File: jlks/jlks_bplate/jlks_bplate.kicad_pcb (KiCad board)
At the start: 2 copper layers, 114.3 x 99.4 mm, 5 parts

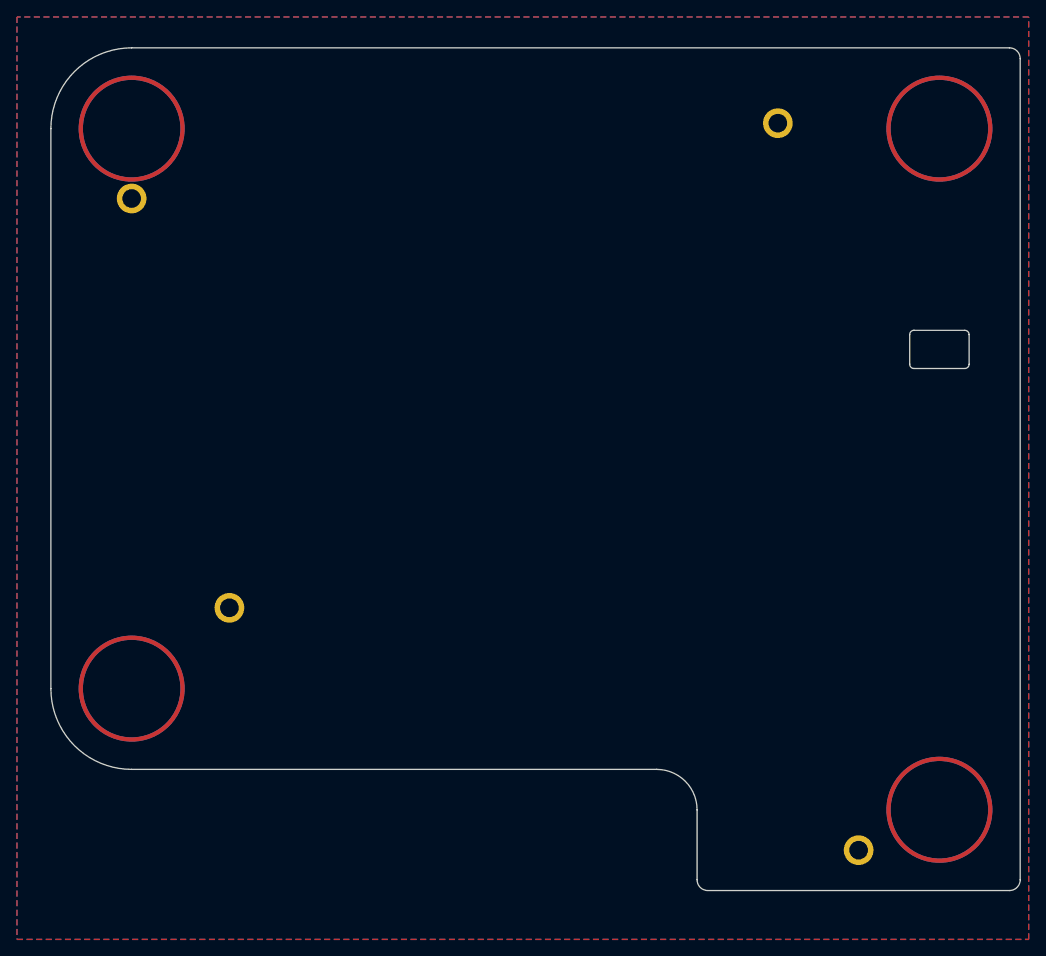
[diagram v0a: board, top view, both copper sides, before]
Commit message: Moved some of the mounting holes around.
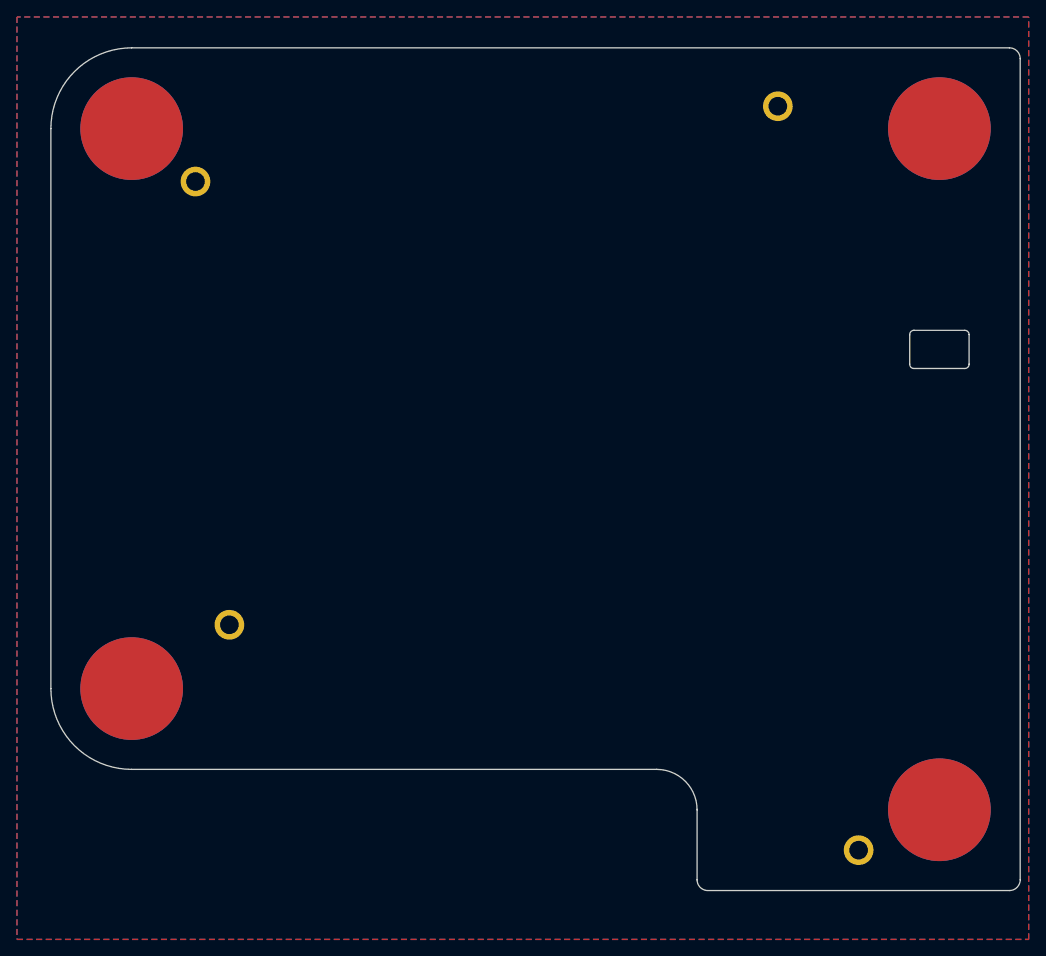
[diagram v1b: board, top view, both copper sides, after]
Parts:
- moved H1 7.79 mm to (74.2, 64.0)
- moved H0 2.00 mm to (142.9, 55.1)
- moved H2 2.00 mm to (78.2, 116.3)
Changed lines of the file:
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@@
   (net 1 "GND")
   (footprint "MountingHole:MountingHole_2.2mm_M2_ISO7380_Pad" (layer "F.Cu")
-    (at 78.2 114.3)
+    (at 78.2 116.3)
     (descr "Mounting Hole 2.2mm, M2, ISO7380")
     (tags "mounting hole 2.2mm m2 iso7380")
@@
   )
   (footprint "MountingHole:MountingHole_2.2mm_M2_ISO7380_Pad" (layer "F.Cu")
-    (at 142.875 57.15)
+    (at 142.875 55.15)
     (descr "Mounting Hole 2.2mm, M2, ISO7380")
     (tags "mounting hole 2.2mm m2 iso7380")
@@
   )
   (footprint "MountingHole:MountingHole_2.2mm_M2_ISO7380_Pad" (layer "F.Cu")
-    (at 66.675 66.033161)
+    (at 74.2 64.033161)
     (descr "Mounting Hole 2.2mm, M2, ISO7380")
     (tags "mounting hole 2.2mm m2 iso7380")
@@
   )
   (gr_circle (center 161.925 138.1125) (end 167.925 138.1125)
-    (stroke (width 0.5) (type default)) (fill none) (layer "F.Cu"))
+    (stroke (width 0.1) (type solid)) (fill solid) (layer "F.Cu"))
   (gr_circle (center 66.675 57.791839) (end 72.675 57.791839)
-    (stroke (width 0.5) (type default)) (fill none) (layer "F.Cu"))
+    (stroke (width 0.1) (type solid)) (fill solid) (layer "F.Cu"))
   (gr_circle (center 66.675 123.825) (end 72.675 123.825)
-    (stroke (width 0.5) (type default)) (fill none) (layer "F.Cu"))
+    (stroke (width 0.1) (type solid)) (fill solid) (layer "F.Cu"))
   (gr_circle (center 161.925 57.791839) (end 167.925 57.791839)
-    (stroke (width 0.5) (type default)) (fill none) (layer "F.Cu"))
+    (stroke (width 0.1) (type solid)) (fill solid) (layer "F.Cu"))
   (gr_circle (center 66.675 123.825) (end 72.675 123.825)
-    (stroke (width 0.5) (type default)) (fill none) (layer "B.Cu"))
+    (stroke (width 0.1) (type solid)) (fill solid) (layer "B.Cu"))
   (gr_circle (center 161.925 138.1125) (end 167.925 138.1125)
-    (stroke (width 0.5) (type default)) (fill none) (layer "B.Cu"))
+    (stroke (width 0.1) (type solid)) (fill solid) (layer "B.Cu"))
   (gr_circle (center 66.675 57.791839) (end 72.675 57.791839)
-    (stroke (width 0.5) (type default)) (fill none) (layer "B.Cu"))
+    (stroke (width 0.1) (type solid)) (fill solid) (layer "B.Cu"))
   (gr_circle (center 161.925 57.791839) (end 167.925 57.791839)
-    (stroke (width 0.5) (type default)) (fill none) (layer "B.Cu"))
+    (stroke (width 0.1) (type solid)) (fill solid) (layer "B.Cu"))
   (gr_arc (start 128.5875 133.35) (mid 131.955096 134.744904) (end 133.35 138.1125)
     (stroke (width 0.1) (type default)) (layer "Edge.Cuts"))

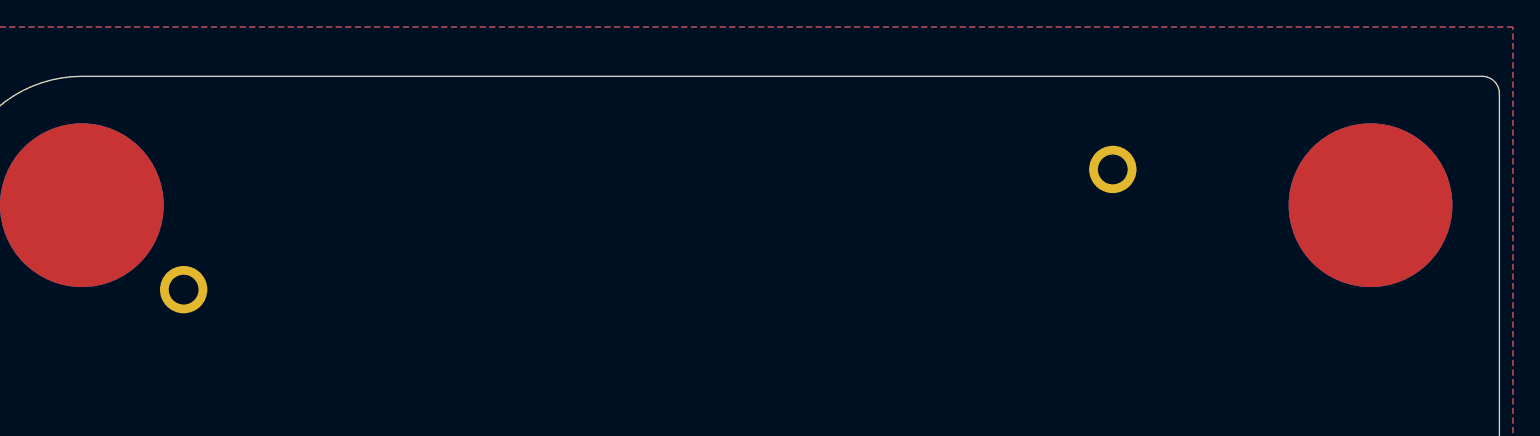
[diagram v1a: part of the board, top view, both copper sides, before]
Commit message: Small modifications to the top and bottom plates.
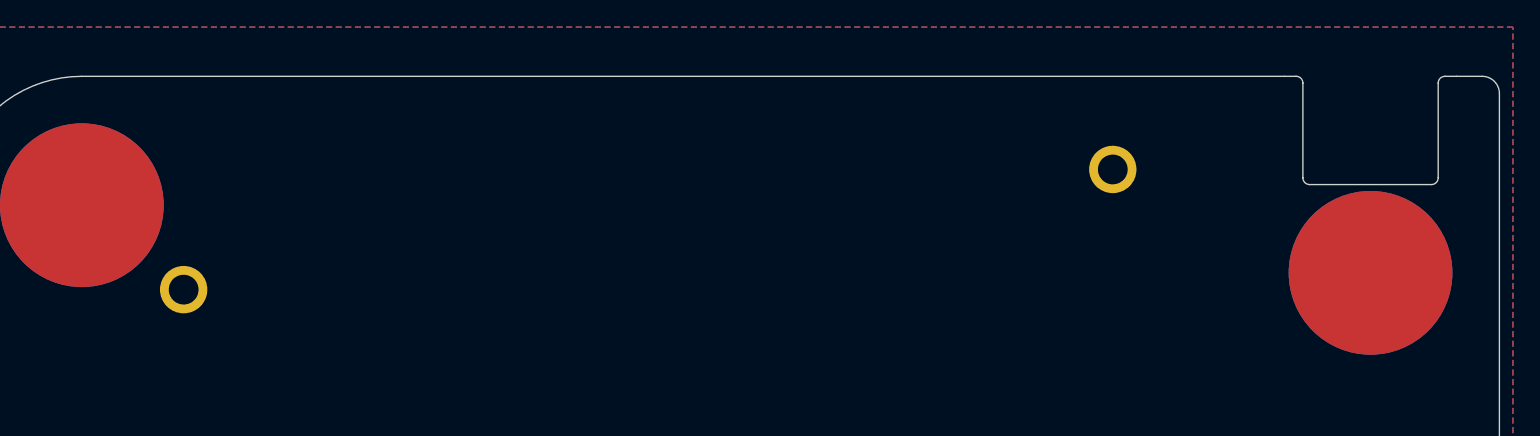
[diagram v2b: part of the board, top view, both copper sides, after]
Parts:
- added U1: ${VALUE}, footprints:nice!nano_usbc_cutout, F.Cu at (161.9, 48.3)
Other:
- outline, holes or cut-outs redrawn
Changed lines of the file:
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@@
     (pad "1" thru_hole circle (at 0 0) (size 3.5 3.5) (drill 2.2) (layers "*.Cu" "*.Mask"))
+  )
+  (footprint "footprints:nice!nano_usbc_cutout" (layer "F.Cu")
+    (at 161.925 48.266839 -90)
+    (attr through_hole)
+    (fp_text reference "U1" (at 17.78 -1.625 90) (layer "F.SilkS") hide
+        (effects (font (size 1.27 1.524) (thickness 0.2032)))
+    )
+    (fp_text value "${VALUE}" (at 17.78 0 90) (layer "F.SilkS") hide
+        (effects (font (size 1.27 1.524) (thickness 0.254) bold))
+    )
+    (fp_line (start 0 -5.5) (end 0 -6.35)
+      (stroke (width 0.1) (type default)) (layer "Edge.Cuts"))
+    (fp_line (start 0 5.5) (end 0 6.35)
+      (stroke (width 0.1) (type default)) (layer "Edge.Cuts"))
+    (fp_line (start 0.5 5) (end 7.5 5)
+      (stroke (width 0.1) (type default)) (layer "Edge.Cuts"))
+    (fp_line (start 7.5 -5) (end 0.5 -5)
+      (stroke (width 0.1) (type default)) (layer "Edge.Cuts"))
+    (fp_line (start 8 4.5) (end 8 -4.5)
+      (stroke (width 0.1) (type default)) (layer "Edge.Cuts"))
+    (fp_arc (start 0 5.5) (mid 0.146447 5.146447) (end 0.5 5)
+      (stroke (width 0.1) (type default)) (layer "Edge.Cuts"))
+    (fp_arc (start 0.5 -5) (mid 0.146447 -5.146447) (end 0 -5.5)
+      (stroke (width 0.1) (type default)) (layer "Edge.Cuts"))
+    (fp_arc (start 7.5 -5) (mid 7.853553 -4.853553) (end 8 -4.5)
+      (stroke (width 0.1) (type default)) (layer "Edge.Cuts"))
+    (fp_arc (start 8 4.5) (mid 7.853553 4.853553) (end 7.5 5)
+      (stroke (width 0.1) (type default)) (layer "Edge.Cuts"))
   )
   (footprint "MountingHole:MountingHole_2.2mm_M2_ISO7380_Pad" (layer "F.Cu")
@@
   (gr_circle (center 66.675 123.825) (end 72.675 123.825)
     (stroke (width 0.1) (type solid)) (fill solid) (layer "F.Cu"))
-  (gr_circle (center 161.925 57.791839) (end 167.925 57.791839)
+  (gr_circle (center 161.925 62.791839) (end 167.925 62.791839)
     (stroke (width 0.1) (type solid)) (fill solid) (layer "F.Cu"))
   (gr_circle (center 66.675 123.825) (end 72.675 123.825)
@@
   (gr_circle (center 66.675 57.791839) (end 72.675 57.791839)
     (stroke (width 0.1) (type solid)) (fill solid) (layer "B.Cu"))
-  (gr_circle (center 161.925 57.791839) (end 167.925 57.791839)
+  (gr_circle (center 161.925 62.791839) (end 167.925 62.791839)
     (stroke (width 0.1) (type solid)) (fill solid) (layer "B.Cu"))
   (gr_arc (start 128.5875 133.35) (mid 131.955096 134.744904) (end 133.35 138.1125)
     (stroke (width 0.1) (type default)) (layer "Edge.Cuts"))
-  (gr_line (start 170.18 48.266839) (end 66.675 48.266839)
+  (gr_line (start 155.575 48.266839) (end 66.675 48.266839)
     (stroke (width 0.1) (type default)) (layer "Edge.Cuts"))
   (gr_arc (start 171.45 146.3675) (mid 171.078026 147.265526) (end 170.18 147.6375)
@@
   (gr_line (start 134.62 147.6375) (end 170.18 147.6375)
     (stroke (width 0.1) (type default)) (layer "Edge.Cuts"))
+  (gr_line (start 168.275 48.266839) (end 170.18 48.266839)
+    (stroke (width 0.1) (type default)) (layer "Edge.Cuts"))
   (zone (net 1) (net_name "GND") (layers "F&B.Cu") (hatch edge 0.5)
